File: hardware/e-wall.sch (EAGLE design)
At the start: 62 parts, among them IC1 74HCT595D, IC2 74HCT595D, IC3 74HCT595D, Q1 BSS123, Q10 BSS123, Q11 BSS123, Q12 BSS123, Q13 BSS123, Q14 BSS123, Q15 BSS123, Q16 BSS123, Q17 BSS123, Q18 BSS123, Q19 BSS123, Q2 BSS123, Q20 BSS123, Q21 BSS123, Q22 BSS123, Q23 BSS123, Q24 BSS123, Q3 BSS123, Q4 BSS123, Q5 BSS123, Q6 BSS123, Q7 BSS123, Q8 BSS123, Q9 BSS123, T1 BC547, T2 BC557, T3 BC547

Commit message: Transistoren BSS123 durch Transistorarrays ULN2803 ersetzt
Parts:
- removed Q1, Q10, Q11, Q12, Q13, Q14, Q15, Q16, Q17, Q18, Q19, Q2, Q20, Q21, Q22, Q23, Q24, Q3, Q4, Q5, Q6, Q7, Q8, Q9: BSS123, transistor-small-signal:BSS123
- removed SV10, SV11, SV12, SV13, SV14, SV15, SV16, SV17, SV18, SV19, SV20, SV21, SV22, SV23, SV24, SV4, SV5, SV6, SV7, SV8, SV9: (no value), con-amp-mt:L02P
- added IC4, IC5, IC6: (no value), uln-udn:ULN2803A
- IC1, IC2, IC3: value 74HCT595D -> 74HCT595N; device 74xx-eu:74HCT595D -> 74xx-eu:74HCT595N
- SV1, SV2, SV3: device con-amp-mt:L02P -> con-lsta:FE08-2
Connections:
- net N$3 renamed SIMO
- net N$31 renamed ECHO_UC
- net N$32 renamed TRIGGER_UC
- net N$4 renamed CLK
- net N$5 renamed EN
- net N$9 renamed SOMI
- removed net N$27: Q24.D, SV24-2.S
- removed net N$28: Q23.D, SV23-2.S
- removed net N$29: Q22.D, SV22-2.S
- removed net N$30: Q21.D, SV21-2.S
- new net N$3: IC6.O1, SV3.2
- new net N$4: IC6.O2, SV3.4
- new net N$5: IC6.O3, SV3.6
- new net N$9: IC6.O7, SV3.14
- net +12V: now also IC4.CD+, IC5.CD+, IC6.CD+, SV1.1, SV1.11, SV1.13, SV1.15, SV1.3, SV1.5, SV1.7, SV1.9, SV2.1, SV2.11, SV2.13, SV2.15, SV2.3, SV2.5, SV2.7, SV2.9, SV3.1, SV3.11, SV3.13, SV3.15, SV3.3, SV3.5, SV3.7, SV3.9; no longer SV1-1.S, SV10-1.S, SV11-1.S, SV12-1.S, SV13-1.S, SV14-1.S, SV15-1.S, SV16-1.S, SV17-1.S, SV18-1.S, SV19-1.S, SV2-1.S, SV20-1.S, SV21-1.S, SV22-1.S, SV23-1.S, SV24-1.S, SV3-1.S, SV4-1.S, SV5-1.S, SV6-1.S, SV7-1.S, SV8-1.S, SV9-1.S
- net GND: now also IC4.GND, IC5.GND, IC6.GND; no longer Q1.S, Q10.S, Q11.S, Q12.S, Q13.S, Q14.S, Q15.S, Q16.S, Q17.S, Q18.S, Q19.S, Q2.S, Q20.S, Q21.S, Q22.S, Q23.S, Q24.S, Q3.S, Q4.S, Q5.S, Q6.S, Q7.S, Q8.S, Q9.S
- net N$10: now also IC6.O8, SV3.16; no longer Q1.D, SV1-2.S
- net N$11: now also IC5.O1, SV2.2; no longer Q8.D, SV8-2.S
- net N$12: now also IC5.O2, SV2.4; no longer Q7.D, SV7-2.S
- net N$13: now also IC5.O3, SV2.6; no longer Q6.D, SV6-2.S
- net N$14: now also IC5.O4, SV2.8; no longer Q5.D, SV5-2.S
- net N$15: now also IC5.O5, SV2.10; no longer Q12.D, SV12-2.S
- net N$16: now also IC5.O6, SV2.12; no longer Q11.D, SV11-2.S
- net N$17: now also IC5.O7, SV2.14; no longer Q10.D, SV10-2.S
- net N$18: now also IC5.O8, SV2.16; no longer Q9.D, SV9-2.S
- net N$19: now also IC4.O1, SV1.2; no longer Q16.D, SV16-2.S
- net N$20: now also IC4.O2, SV1.4; no longer Q15.D, SV15-2.S
- net N$21: now also IC4.O3, SV1.6; no longer Q14.D, SV14-2.S
- net N$22: now also IC4.O4, SV1.8; no longer Q13.D, SV13-2.S
- net N$23: now also IC4.O5, SV1.10; no longer Q20.D, SV20-2.S
- net N$24: now also IC4.O6, SV1.12; no longer Q19.D, SV19-2.S
- net N$25: now also IC4.O7, SV1.14; no longer Q18.D, SV18-2.S
- net N$26: now also IC4.O8, SV1.16; no longer Q17.D, SV17-2.S
- net N$6: now also IC6.O4, SV3.8; no longer Q4.D, SV4-2.S
- net N$7: now also IC6.O5, SV3.10; no longer Q3.D, SV3-2.S
- net N$8: now also IC6.O6, SV3.12; no longer Q2.D, SV2-2.S
- net OUT0: now also IC4.I8; no longer Q1.G
- net OUT1: now also IC4.I7; no longer Q2.G
- net OUT10: now also IC5.I6; no longer Q11.G
- net OUT11: now also IC5.I5; no longer Q12.G
- net OUT12: now also IC5.I4; no longer Q13.G
- net OUT13: now also IC5.I3; no longer Q14.G
- net OUT14: now also IC5.I2; no longer Q15.G
- net OUT15: now also IC5.I1; no longer Q16.G
- net OUT16: now also IC6.I8; no longer Q17.G
- net OUT17: now also IC6.I7; no longer Q18.G
- net OUT18: now also IC6.I6; no longer Q19.G
- net OUT19: now also IC6.I5; no longer Q20.G
- net OUT2: now also IC4.I6; no longer Q3.G
- net OUT20: now also IC6.I4; no longer Q21.G
- net OUT21: now also IC6.I3; no longer Q22.G
- net OUT22: now also IC6.I2; no longer Q23.G
- net OUT23: now also IC6.I1; no longer Q24.G
- net OUT3: now also IC4.I5; no longer Q4.G
- net OUT4: now also IC4.I4; no longer Q5.G
- net OUT5: now also IC4.I3; no longer Q6.G
- net OUT6: now also IC4.I2; no longer Q7.G
- net OUT7: now also IC4.I1; no longer Q8.G
- net OUT8: now also IC5.I8; no longer Q9.G
- net OUT9: now also IC5.I7; no longer Q10.G

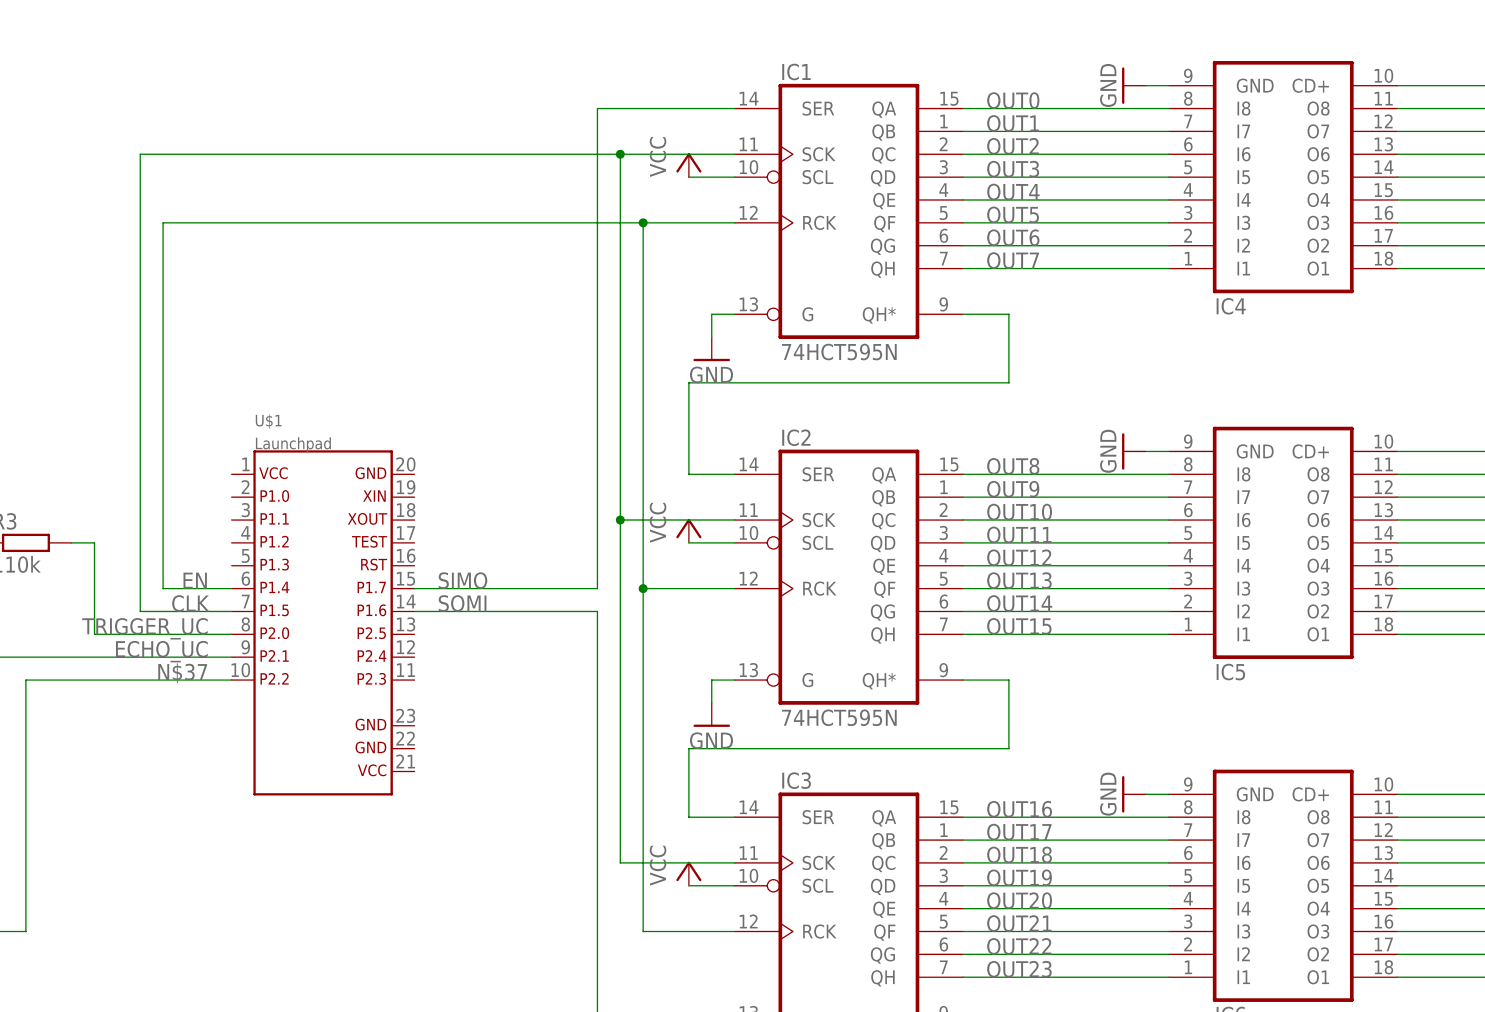
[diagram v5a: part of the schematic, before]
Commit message: SMD Bauteile durch THT ersetzt
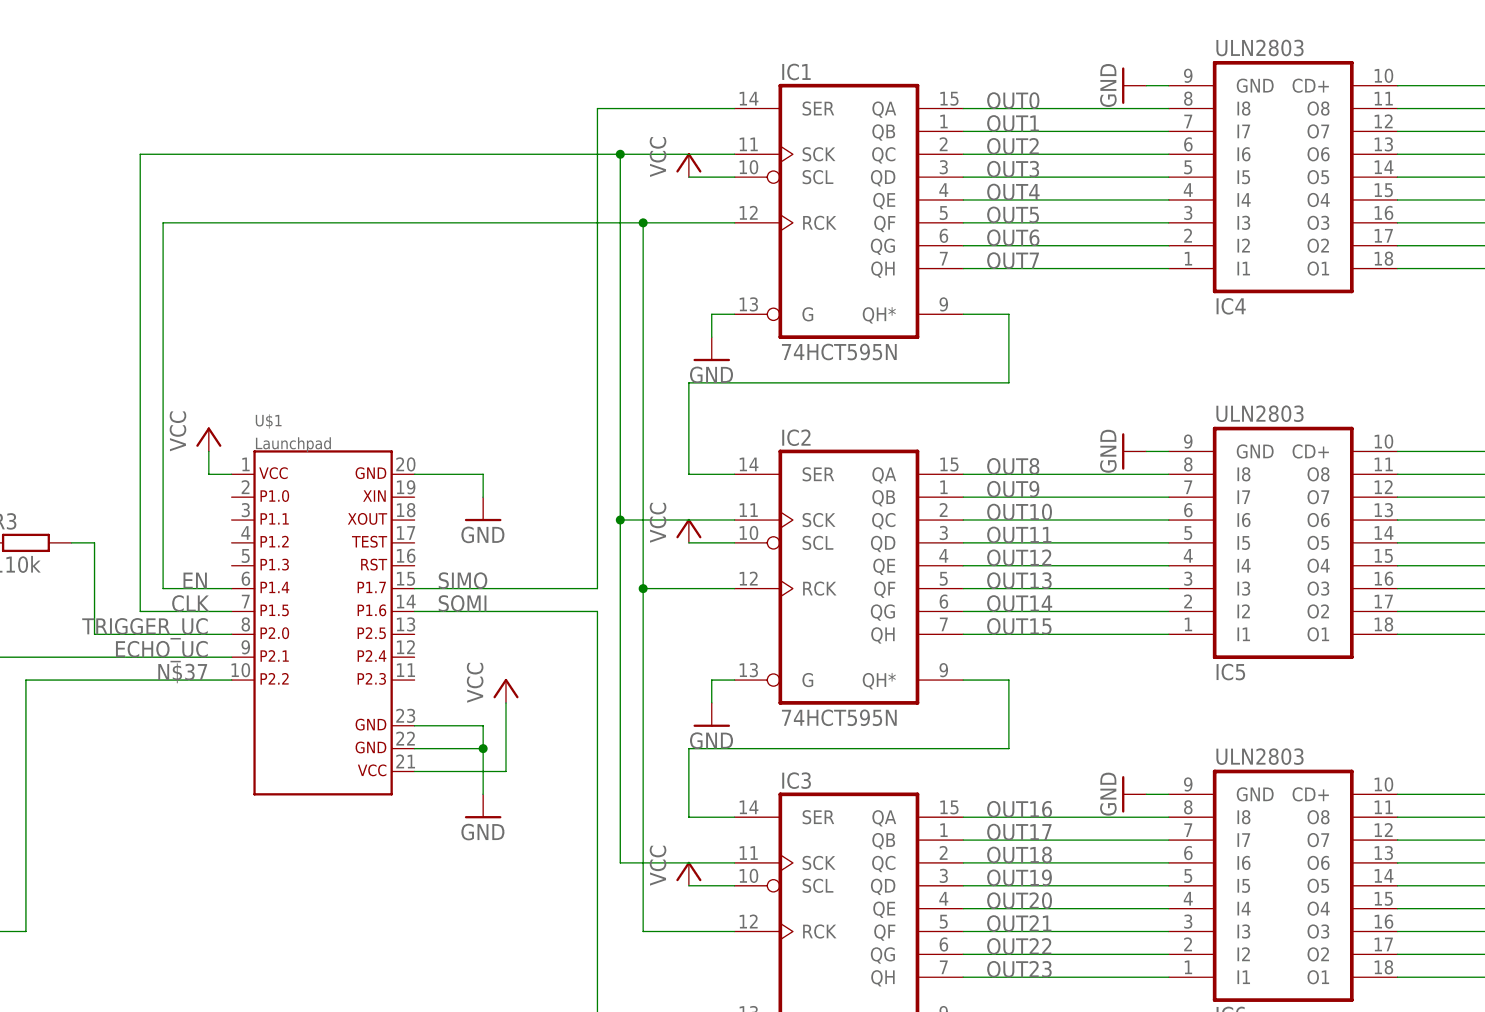
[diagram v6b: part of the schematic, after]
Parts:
- IC4, IC5, IC6: value (none) -> ULN2803
- R1, R2, R3, R4, R5, R6, R7: device resistor:R-EU_R0805 -> resistor:R-EU_0309/10
- T1, T3: device transistor:-NPN-SOT23-EBC -> transistor:-NPN-TO92-EBC
- T2: device transistor:-PNP-SOT23-EBC -> transistor:-PNP-TO92-BEC
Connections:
- net GND: now also U$1.20, U$1.22, U$1.23
- net VCC: now also U$1.1, U$1.21
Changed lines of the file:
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@@
 <setting verticaltext="up"/>
 </settings>
-<grid distance="0.1" unitdist="inch" unit="inch" style="dots" multiple="1" display="yes" altdistance="0.01" altunitdist="inch" altunit="inch"/>
+<grid distance="0.1" unitdist="inch" unit="inch" style="lines" multiple="1" display="no" altdistance="0.01" altunitdist="inch" altunit="inch"/>
 <layers>
 <layer number="1" name="Top" color="4" fill="1" visible="yes" active="no"/>
@@
 <part name="GND8" library="supply1" deviceset="GND" device=""/>
 <part name="P+8" library="supply1" deviceset="+12V" device=""/>
-<part name="R1" library="resistor" deviceset="R-EU_" device="R0805" value="20k"/>
-<part name="R2" library="resistor" deviceset="R-EU_" device="R0805" value="30k"/>
-<part name="R3" library="resistor" deviceset="R-EU_" device="R0805" value="110k"/>
-<part name="R4" library="resistor" deviceset="R-EU_" device="R0805" value="NB"/>
-<part name="T1" library="transistor" deviceset="*-NPN-" device="SOT23-EBC" value="BC547"/>
+<part name="R1" library="resistor" deviceset="R-EU_" device="0309/10" value="20k"/>
+<part name="R2" library="resistor" deviceset="R-EU_" device="0309/10" value="30k"/>
+<part name="R3" library="resistor" deviceset="R-EU_" device="0309/10" value="110k"/>
+<part name="R4" library="resistor" deviceset="R-EU_" device="0309/10" value="NB"/>
+<part name="T1" library="transistor" deviceset="*-NPN-" device="TO92-EBC" value="BC547"/>
 <part name="GND28" library="supply1" deviceset="GND" device=""/>
 <part name="GND29" library="supply1" deviceset="GND" device=""/>
 <part name="P+28" library="supply1" deviceset="VCC" device=""/>
-<part name="T2" library="transistor" deviceset="*-PNP-" device="SOT23-EBC" value="BC557"/>
-<part name="R6" library="resistor" deviceset="R-EU_" device="R0805" value="4.7k"/>
+<part name="T2" library="transistor" deviceset="*-PNP-" device="TO92-BEC" value="BC557"/>
+<part name="R6" library="resistor" deviceset="R-EU_" device="0309/10" value="4.7k"/>
 <part name="GND30" library="supply1" deviceset="GND" device=""/>
 <part name="P+29" library="supply1" deviceset="VCC" device=""/>
-<part name="R5" library="resistor" deviceset="R-EU_" device="R0805" value="6.2k"/>
-<part name="T3" library="transistor" deviceset="*-NPN-" device="SOT23-EBC" value="BC547"/>
-<part name="R7" library="resistor" deviceset="R-EU_" device="R0805" value="7.5k"/>
+<part name="R5" library="resistor" deviceset="R-EU_" device="0309/10" value="6.2k"/>
+<part name="T3" library="transistor" deviceset="*-NPN-" device="TO92-EBC" value="BC547"/>
+<part name="R7" library="resistor" deviceset="R-EU_" device="0309/10" value="7.5k"/>
 <part name="GND31" library="supply1" deviceset="GND" device=""/>
 <part name="SV1" library="con-lsta" deviceset="FE08-2" device=""/>
@@
 <part name="SV3" library="con-lsta" deviceset="FE08-2" device=""/>
 <part name="GND5" library="supply1" deviceset="GND" device=""/>
-<part name="IC4" library="uln-udn" deviceset="ULN2803A" device=""/>
-<part name="IC5" library="uln-udn" deviceset="ULN2803A" device=""/>
-<part name="IC6" library="uln-udn" deviceset="ULN2803A" device=""/>
+<part name="IC4" library="uln-udn" deviceset="ULN2803A" device="" value="ULN2803"/>
+<part name="IC5" library="uln-udn" deviceset="ULN2803A" device="" value="ULN2803"/>
+<part name="IC6" library="uln-udn" deviceset="ULN2803A" device="" value="ULN2803"/>
+<part name="GND6" library="supply1" deviceset="GND" device=""/>
+<part name="GND7" library="supply1" deviceset="GND" device=""/>
+<part name="P+4" library="supply1" deviceset="VCC" device=""/>
+<part name="P+5" library="supply1" deviceset="VCC" device=""/>
 </parts>
 <sheets>
@@
 <instance part="IC5" gate="G$1" x="185.42" y="66.04" rot="MR180"/>
 <instance part="IC6" gate="G$1" x="185.42" y="27.94" rot="MR180"/>
+<instance part="GND6" gate="1" x="96.52" y="35.56"/>
+<instance part="GND7" gate="1" x="96.52" y="68.58"/>
+<instance part="P+4" gate="VCC" x="66.04" y="78.74"/>
+<instance part="P+5" gate="VCC" x="99.06" y="50.8"/>
 </instances>
 <busses>
@@
 <pinref part="IC4" gate="G$1" pin="GND"/>
 <wire x1="170.18" y1="116.84" x2="172.72" y2="116.84" width="0.1524" layer="91"/>
+</segment>
+<segment>
+<pinref part="U$1" gate="G$1" pin="20"/>
+<pinref part="GND7" gate="1" pin="GND"/>
+<wire x1="88.9" y1="73.66" x2="96.52" y2="73.66" width="0.1524" layer="91"/>
+<wire x1="96.52" y1="73.66" x2="96.52" y2="71.12" width="0.1524" layer="91"/>
+</segment>
+<segment>
+<pinref part="U$1" gate="G$1" pin="23"/>
+<pinref part="GND6" gate="1" pin="GND"/>
+<wire x1="88.9" y1="45.72" x2="96.52" y2="45.72" width="0.1524" layer="91"/>
+<wire x1="96.52" y1="45.72" x2="96.52" y2="43.18" width="0.1524" layer="91"/>
+<pinref part="U$1" gate="G$1" pin="22"/>
+<wire x1="96.52" y1="43.18" x2="96.52" y2="38.1" width="0.1524" layer="91"/>
+<wire x1="88.9" y1="43.18" x2="96.52" y2="43.18" width="0.1524" layer="91"/>
+<junction x="96.52" y="43.18"/>
 </segment>
 </net>
@@
 <wire x1="33.02" y1="88.9" x2="33.02" y2="83.82" width="0.1524" layer="91"/>
 </segment>
-</net>
+<segment>
+<pinref part="P+4" gate="VCC" pin="VCC"/>
+<wire x1="66.04" y1="76.2" x2="66.04" y2="73.66" width="0.1524" layer="91"/>
+<pinref part="U$1" gate="G$1" pin="1"/>
+<wire x1="66.04" y1="73.66" x2="68.58" y2="73.66" width="0.1524" layer="91"/>
+</segment>
+<segment>
+<pinref part="U$1" gate="G$1" pin="21"/>
+<pinref part="P+5" gate="VCC" pin="VCC"/>
+<wire x1="88.9" y1="40.64" x2="99.06" y2="40.64" width="0.1524" layer="91"/>
+<wire x1="99.06" y1="40.64" x2="99.06" y2="48.26" width="0.1524" layer="91"/>
+</segment>
+</net>
